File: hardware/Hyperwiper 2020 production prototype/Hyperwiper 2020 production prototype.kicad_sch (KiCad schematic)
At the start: 22 parts, among them J1 Conn_01x05, J2 USB_B, Q2 2N3904, Q3 IRF4905, SW1 SW_DPDT_x2, SW2 SW_Reed, U1 Teensy4.0, U3 Voltage regulator

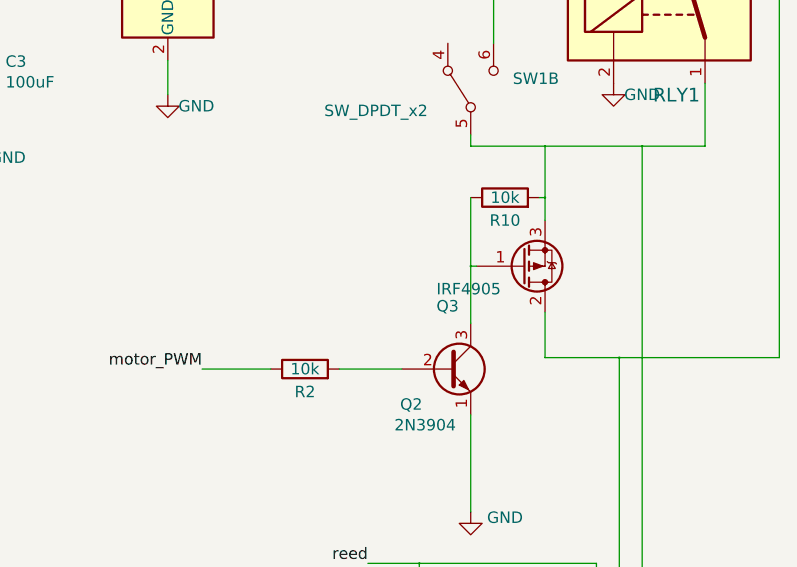
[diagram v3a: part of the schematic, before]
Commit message: Updated code for better delay timing pot meter
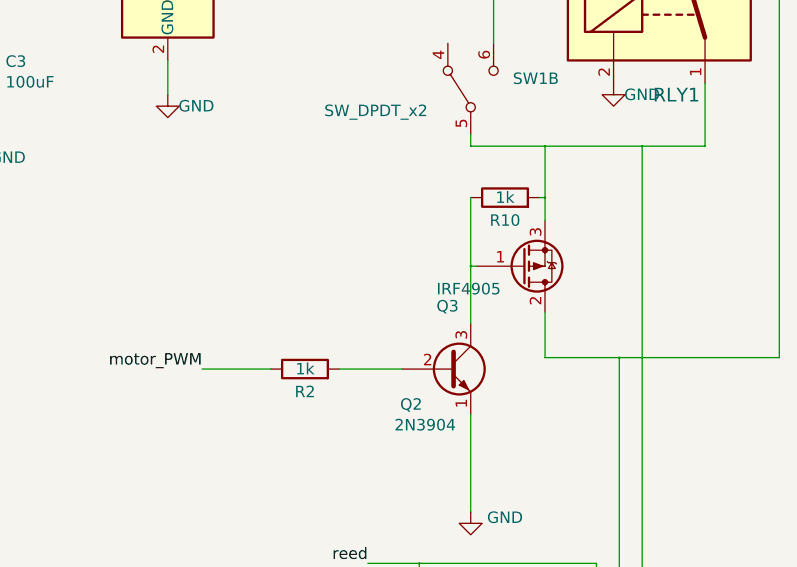
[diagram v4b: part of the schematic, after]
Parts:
- R10, R2: value 10k -> 1k
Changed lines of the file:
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@@
     (in_bom yes) (on_board yes)
     (property "Reference" "R2" (id 0) (at 229.235 90.805 90))
-    (property "Value" "10k" (id 1) (at 229.235 88.265 90))
+    (property "Value" "1k" (id 1) (at 229.235 88.265 90))
     (property "Footprint" "Resistor_THT:R_Axial_DIN0207_L6.3mm_D2.5mm_P10.16mm_Horizontal" (id 2) (at 229.235 90.043 90)
       (effects (font (size 1.27 1.27)) hide)
@@
     (in_bom yes) (on_board yes)
     (property "Reference" "R10" (id 0) (at 251.46 71.755 90))
-    (property "Value" "10k" (id 1) (at 251.46 69.215 90))
+    (property "Value" "1k" (id 1) (at 251.46 69.215 90))
     (property "Footprint" "Resistor_THT:R_Axial_DIN0207_L6.3mm_D2.5mm_P10.16mm_Horizontal" (id 2) (at 251.46 70.993 90)
       (effects (font (size 1.27 1.27)) hide)
@@
     )
     (path "/1fcecf2b-4e2f-4005-a609-f08496f7cf92"
-      (reference "R2") (unit 1) (value "10k") (footprint "Resistor_THT:R_Axial_DIN0207_L6.3mm_D2.5mm_P10.16mm_Horizontal")
+      (reference "R2") (unit 1) (value "1k") (footprint "Resistor_THT:R_Axial_DIN0207_L6.3mm_D2.5mm_P10.16mm_Horizontal")
     )
     (path "/262574bc-5200-41bf-819f-e4ebc4aa93eb"
-      (reference "R10") (unit 1) (value "10k") (footprint "Resistor_THT:R_Axial_DIN0207_L6.3mm_D2.5mm_P10.16mm_Horizontal")
+      (reference "R10") (unit 1) (value "1k") (footprint "Resistor_THT:R_Axial_DIN0207_L6.3mm_D2.5mm_P10.16mm_Horizontal")
     )
     (path "/9655f52e-d83d-4b34-981f-5781f9027fde"

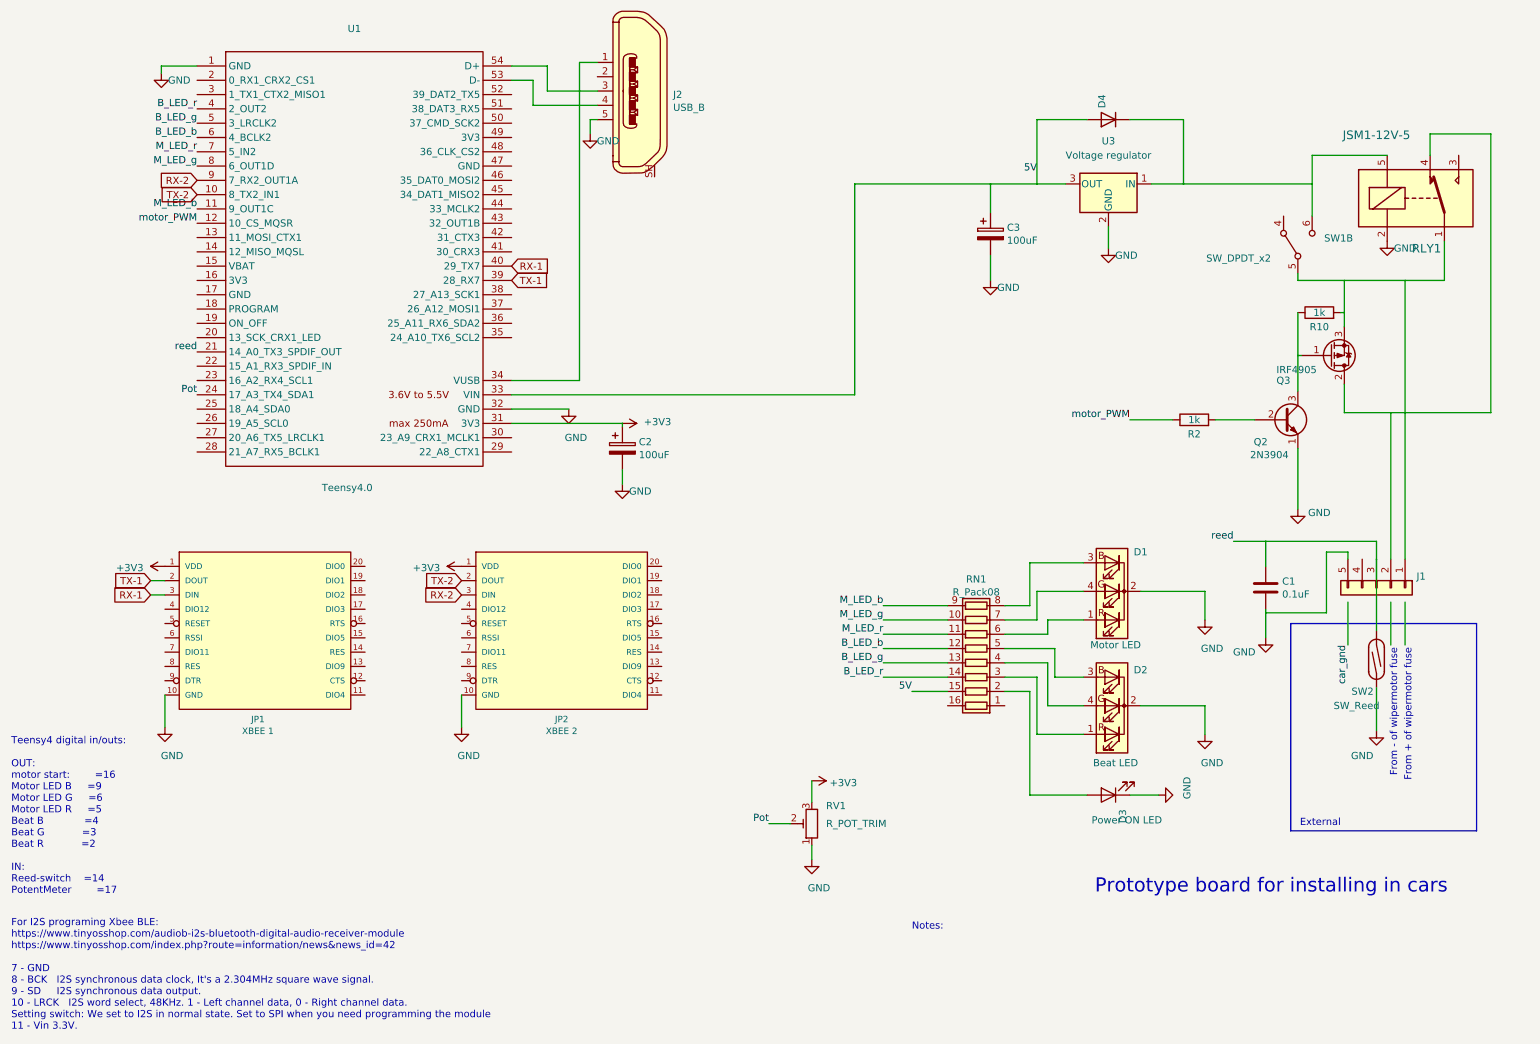
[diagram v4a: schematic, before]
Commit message: Updated schematic for N-CH MOSFET  switching
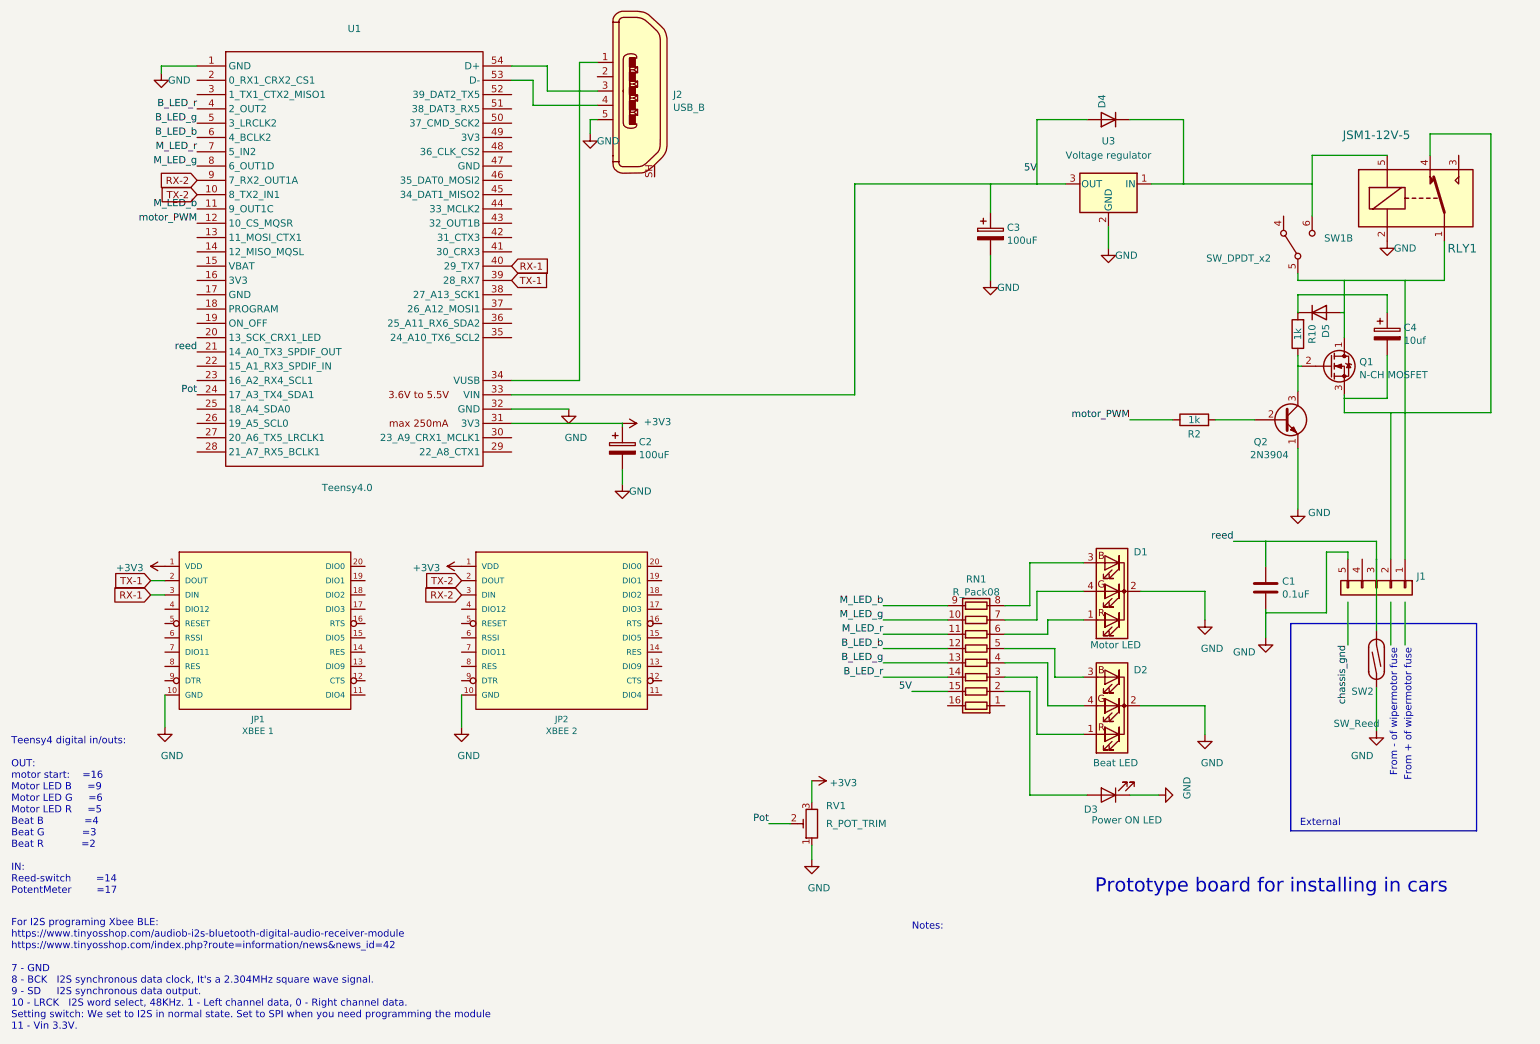
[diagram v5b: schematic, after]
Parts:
- removed Q3: IRF4905, Package_TO_SOT_THT:TO-220-3_Vertical, symbol Transistor_FET:IRF4905
- added C4: 10uf, Capacitor_THT:CP_Radial_D5.0mm_P2.50mm, symbol Device:CP
- added D5: DIODE, Diode_THT:D_DO-35_SOD27_P10.16mm_Horizontal, symbol Simulation_SPICE:DIODE
- added Q1: N-CH MOSFET, Package_DirectFET:DirectFET_MX, symbol Transistor_FET:BSB008NE2LX
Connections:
- net at J1.1 (Pin_1), RLY1.1, SW1.5 (B): now also D5.1 (A), Q1.1 (D); no longer R10.2
- net at J1.2 (Pin_2), RLY1.4: now also C4.2, Q1.3 (S)
- net at Q2.3 (C), R10.1: now also Q1.2 (G)
- new net: C4.1, D5.2 (K), R10.2
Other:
- moved on the sheet: R10

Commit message: Updates board
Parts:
- removed Q1: N-CH MOSFET, Package_DirectFET:DirectFET_MX, symbol Transistor_FET:BSB008NE2LX
- added Q1: IRF3205, Package_TO_SOT_THT:TO-220-3_Vertical, symbol Transistor_FET:IRF3205
- C4: value 10uf -> 100uf
- D5: value DIODE -> 1n4001
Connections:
- net at D5.1 (A), J1.1 (Pin_1), RLY1.1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: now also Q1.2 (D)
- net at C4.2, J1.2 (Pin_2), RLY1.4: now also Q1.3 (S)
- net at Q2.3 (C), R10.1: now also Q1.1 (G)
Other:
- moved on the sheet: C4, D5, Q2, R10, R2

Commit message: Updated board with protection diode and fixed some routing issues.
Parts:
- added D6: 1N4001, Diode_THT:D_DO-35_SOD27_P10.16mm_Horizontal, symbol Simulation_SPICE:DIODE
- D5: value 1n4001 -> 1N4001
- R2: value 1k -> 10k
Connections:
- net GND: now also D6.1 (A)
- net at C4.2, J1.2 (Pin_2), Q1.3 (S)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: now also D6.2 (K)
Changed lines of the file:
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@@
   (junction (at 247.65 73.025) (diameter 0.259) (color 0 0 0 0))
   (junction (at 247.65 84.455) (diameter 0.259) (color 0 0 0 0))
+  (junction (at 247.65 102.87) (diameter 0.259) (color 0 0 0 0))
   (junction (at 250.19 46.355) (diameter 0.259) (color 0 0 0 0))
   (junction (at 255.905 63.5) (diameter 0.259) (color 0 0 0 0))
   (junction (at 255.905 74.93) (diameter 0.259) (color 0 0 0 0))
+  (junction (at 255.905 92.71) (diameter 0.259) (color 0 0 0 0))
   (junction (at 261.62 113.03) (diameter 0.259) (color 0 0 0 0))
   (junction (at 263.525 92.71) (diameter 0.259) (color 0 0 0 0))
@@
     (stroke (width 0) (type solid) (color 0 0 0 0))
   )
-  (wire (pts (xy 247.65 97.79) (xy 247.65 104.14))
+  (wire (pts (xy 247.65 97.79) (xy 247.65 102.87))
+    (stroke (width 0) (type solid) (color 0 0 0 0))
+  )
+  (wire (pts (xy 247.65 102.87) (xy 247.65 104.14))
+    (stroke (width 0) (type solid) (color 0 0 0 0))
+  )
+  (wire (pts (xy 247.65 102.87) (xy 255.905 102.87))
     (stroke (width 0) (type solid) (color 0 0 0 0))
   )
@@
   )
   (wire (pts (xy 255.905 89.535) (xy 255.905 92.71))
+    (stroke (width 0) (type solid) (color 0 0 0 0))
+  )
+  (wire (pts (xy 255.905 92.71) (xy 255.905 95.25))
     (stroke (width 0) (type solid) (color 0 0 0 0))
   )
@@
     (in_bom yes) (on_board yes)
     (property "Reference" "R2" (id 0) (at 229.235 95.25 90))
-    (property "Value" "1k" (id 1) (at 229.235 92.71 90))
+    (property "Value" "10k" (id 1) (at 229.235 92.71 90))
     (property "Footprint" "Resistor_THT:R_Axial_DIN0207_L6.3mm_D2.5mm_P10.16mm_Horizontal" (id 2) (at 229.235 94.488 90)
       (effects (font (size 1.27 1.27)) hide)
@@
       (effects (font (size 1.27 1.27)) (justify left))
     )
-    (property "Value" "1n4001" (id 1) (at 249.682 68.459 90)
-      (effects (font (size 1.27 1.27)) (justify left) hide)
+    (property "Value" "1N4001" (id 1) (at 249.682 68.459 90)
+      (effects (font (size 1.27 1.27)) (justify left))
     )
     (property "Footprint" "Diode_THT:D_DO-35_SOD27_P10.16mm_Horizontal" (id 2) (at 247.65 67.31 0)
@@
     )
     (property "Spice_Primitive" "V" (id 5) (at 247.65 67.31 0)
+      (effects (font (size 1.27 1.27)) (justify left) hide)
+    )
+    (pin "1")
+    (pin "2")
+  )
+  (symbol (lib_id "Simulation_SPICE:DIODE") (at 255.905 99.06 90) (unit 1)
+    (in_bom yes) (on_board yes)
+    (property "Reference" "D6" (id 0) (at 253.8729 100.2094 90)
+      (effects (font (size 1.27 1.27)) (justify left))
+    )
+    (property "Value" "1N4001" (id 1) (at 262.763 104.261 90)
+      (effects (font (size 1.27 1.27)) (justify left))
+    )
+    (property "Footprint" "Diode_THT:D_DO-35_SOD27_P10.16mm_Horizontal" (id 2) (at 255.905 99.06 0)
+      (effects (font (size 1.27 1.27)) hide)
+    )
+    (property "Datasheet" "~" (id 3) (at 255.905 99.06 0)
+      (effects (font (size 1.27 1.27)) hide)
+    )
+    (property "Spice_Netlist_Enabled" "Y" (id 4) (at 255.905 99.06 0)
+      (effects (font (size 1.27 1.27)) (justify left) hide)
+    )
+    (property "Spice_Primitive" "V" (id 5) (at 255.905 99.06 0)
       (effects (font (size 1.27 1.27)) (justify left) hide)
     )
@@
     )
     (path "/04d453a9-1705-44d3-9ebf-0298cab79c16"
-      (reference "D5") (unit 1) (value "1n4001") (footprint "Diode_THT:D_DO-35_SOD27_P10.16mm_Horizontal")
+      (reference "D5") (unit 1) (value "1N4001") (footprint "Diode_THT:D_DO-35_SOD27_P10.16mm_Horizontal")
+    )
+    (path "/1a312573-7d03-4590-afd1-c986b8947736"
+      (reference "D6") (unit 1) (value "1N4001") (footprint "Diode_THT:D_DO-35_SOD27_P10.16mm_Horizontal")
     )
     (path "/25cecf71-7aa2-492f-89ca-2aaf0234512e"
@@
     )
     (path "/1fcecf2b-4e2f-4005-a609-f08496f7cf92"
-      (reference "R2") (unit 1) (value "1k") (footprint "Resistor_THT:R_Axial_DIN0207_L6.3mm_D2.5mm_P10.16mm_Horizontal")
+      (reference "R2") (unit 1) (value "10k") (footprint "Resistor_THT:R_Axial_DIN0207_L6.3mm_D2.5mm_P10.16mm_Horizontal")
     )
     (path "/262574bc-5200-41bf-819f-e4ebc4aa93eb"

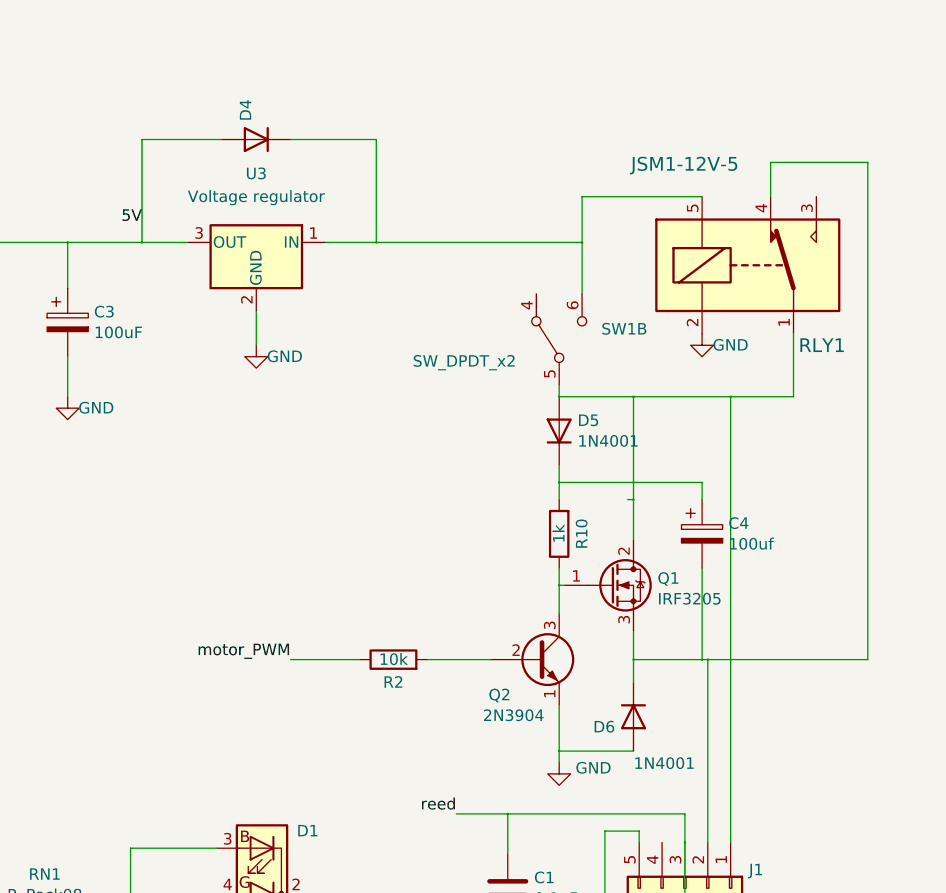
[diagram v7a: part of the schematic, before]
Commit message: Changed LM7805 to OKI-78SR
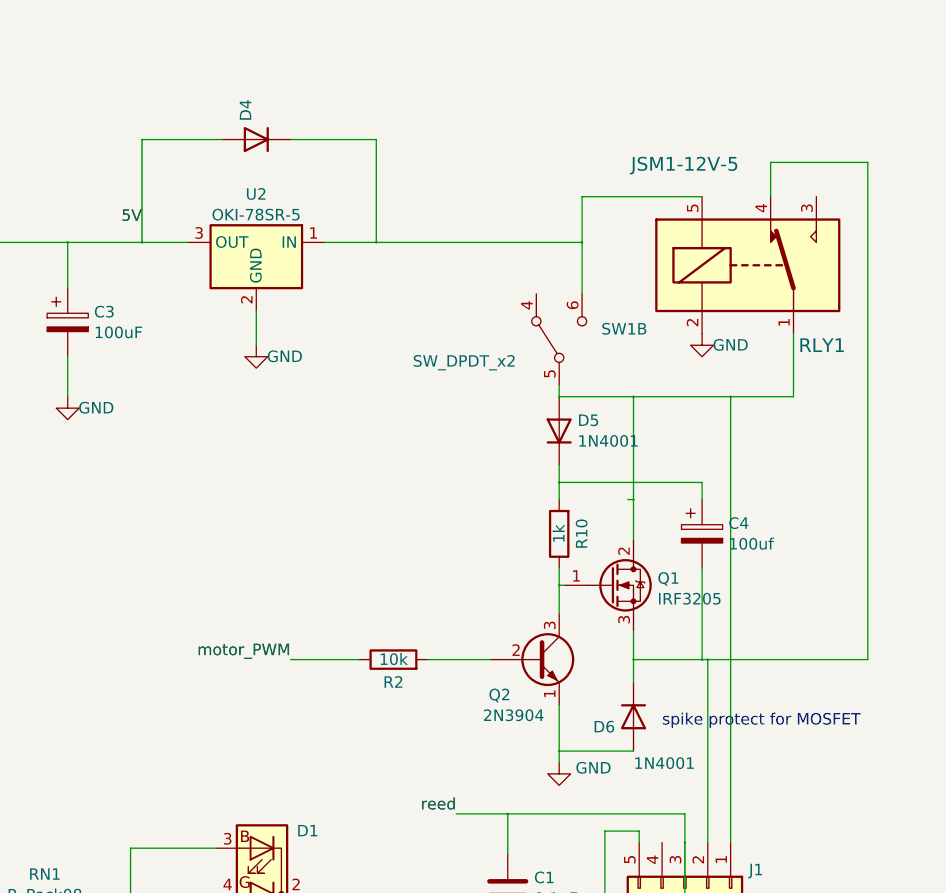
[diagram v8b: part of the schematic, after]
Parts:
- removed U3: Voltage regulator, Package_TO_SOT_THT:TO-220-3_Vertical, symbol Regulator_Linear:L7805
- added U2: OKI-78SR-5, Converter_DCDC:Converter_DCDC_muRata_OKI-78SR_Horizontal, symbol Converter_DCDC:OKI-78SR-3.3_1.5-W36H-C
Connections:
- net 5V: now also U2.3 (OUT)
- net GND: now also U2.2 (GND)
- net at D4.2 (K), RLY1.5, SW1.6 (C): now also U2.1 (IN)
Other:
- note added: "spike protect for MOSFET"
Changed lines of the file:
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@@
     (effects (font (size 1.27 1.27)) (justify right bottom))
+  )
+  (text "spike protect for MOSFET" (at 259.08 100.33 0)
+    (effects (font (size 1.27 1.27)) (justify left bottom))
   )
   (text "From - of wipermotor fuse\n" (at 265.43 128.905 270)
@@
     (pin "3")
   )
-  (symbol (lib_id "Regulator_Linear:L7805") (at 213.995 46.355 0) (mirror y) (unit 1)
-    (in_bom yes) (on_board yes)
-    (property "Reference" "U3" (id 0) (at 213.995 38.735 0))
-    (property "Value" "Voltage regulator" (id 1) (at 213.995 41.275 0))
-    (property "Footprint" "Package_TO_SOT_THT:TO-220-3_Vertical" (id 2) (at 213.36 50.165 0)
+  (symbol (lib_id "Converter_DCDC:OKI-78SR-3.3_1.5-W36H-C") (at 213.995 46.355 0) (mirror y) (unit 1)
+    (in_bom yes) (on_board yes) (fields_autoplaced)
+    (property "Reference" "U2" (id 0) (at 213.995 41.0168 0))
+    (property "Value" "OKI-78SR-5" (id 1) (at 213.995 43.3155 0))
+    (property "Footprint" "Converter_DCDC:Converter_DCDC_muRata_OKI-78SR_Horizontal" (id 2) (at 212.725 52.705 0)
       (effects (font (size 1.27 1.27) italic) (justify left) hide)
     )
-    (property "Datasheet" "http://www.st.com/content/ccc/resource/technical/document/datasheet/41/4f/b3/b0/12/d4/47/88/CD00000444.pdf/files/CD00000444.pdf/jcr:content/translations/en.CD00000444.pdf" (id 3) (at 213.995 47.625 0)
+    (property "Datasheet" "https://power.murata.com/data/power/oki-78sr.pdf" (id 3) (at 213.995 46.355 0)
       (effects (font (size 1.27 1.27)) hide)
     )
@@
       (reference "U1") (unit 1) (value "Teensy4.0") (footprint "Hyperwiper 2020 production prototype all:Teensy40")
     )
-    (path "/f9d2509a-a206-4349-9d2a-528f7b1ec6de"
-      (reference "U3") (unit 1) (value "Voltage regulator") (footprint "Package_TO_SOT_THT:TO-220-3_Vertical")
-    )
-  )
+    (path "/4d72a9e6-3dfe-4052-a8a0-f178950332cc"
+      (reference "U2") (unit 1) (value "OKI-78SR-5") (footprint "Converter_DCDC:Converter_DCDC_muRata_OKI-78SR_Horizontal")
+    )
+  )
